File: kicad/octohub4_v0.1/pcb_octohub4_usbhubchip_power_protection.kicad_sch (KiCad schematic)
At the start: 16 parts, among them J201 Screw_Terminal_01x02, J203 Barrel_Jack_Switch, U201 TPS259474LRPWR

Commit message: Add run_kicad_purge 2
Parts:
- added JP201, JP202: SolderJumper_2_Bridged, Jumper:SolderJumper-2_P1.3mm_Bridged_RoundedPad1.0x1.5mm, symbol Jumper:SolderJumper_2_Bridged
- added JP205: SolderJumper_2_Open, Jumper:SolderJumper-2_P1.3mm_Open_RoundedPad1.0x1.5mm, symbol Jumper:SolderJumper_2_Open
- added TH1301, TH1302: JLCPCB Tooling Hole, 00_project_library:JLCPCB_ToolingHole, symbol 00_project_library:JLCPCB_ToolingHole
- BP201, BP202: footprint SolderWirePad_1x01_SMD_2x4mm -> Connector_Wire:SolderWirePad_1x01_SMD_2x4mm
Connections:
- net +5VIN: now also JP201.1 (A), JP202.1 (A), JP205.2 (B); no longer H201.1, H202.1
- net +5VOUT renamed +5VPROTECTED
- net +5VPROTECTED: now also JP205.1 (A)
- new net: H202.1, JP202.2 (B)
- new net: H201.1, JP201.2 (B)
- no-connect marks 0 -> 2
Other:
- moved on the sheet: H1301, H1302, H201, H202

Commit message: Add run_kicad_purge 3
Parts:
- added D207: green, LED_SMD:LED_0805_2012Metric, symbol 00_project_library:LED GREEN
- added R202: 4K7, Resistor_SMD:R_0805_2012Metric, symbol Device:R
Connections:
- net +5VIN: now also J201.2 (Pin_2); no longer J201.1 (Pin_1)
- net +5VPROTECTED: now also R202.2
- net GND: now also J201.1 (Pin_1), D207.1 (K); no longer J201.2 (Pin_2)
- new net: D207.2 (A), R202.1
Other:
- note added: "5VPROTECTED LED"
- moved on the sheet: J201

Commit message: Add run_kicad_purge 4
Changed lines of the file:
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@@
-	(wire
-		(pts
-			(xy 80.01 97.79) (xy 80.01 102.87)
-		)
-		(stroke
-			(width 0)
-			(type default)
-		)
-	)
 	(wire
 		(pts

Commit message: Add run_kicad_purge 5
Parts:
- J201: now left out of the parts list
- R201: value 137 -> 120
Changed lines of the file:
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@@
 		)
 	)
-	(text_box "R201: Current limit ~4.47A (612 / 137 Ohm)\nC203: Allows transient surges (up to 2x limit) for ~6ms.\nC202: Output voltage ramp time to 5V/500ms"
+	(text_box "R201: Current limit ~5.1A (612 / 120 Ohm)\nC203: Allows transient surges (up to 2x limit) for ~6ms.\nC202: Output voltage ramp time to 5V/500ms"
 		(exclude_from_sim no)
 		(at 92.71 128.27 0)
@@
 			)
 		)
-		(property "Value" "137"
+		(property "Value" "120"
 			(at 158.6484 111.76 90)
 			(effects
@@
 		(unit 1)
 		(exclude_from_sim no)
-		(in_bom yes)
-		(on_board yes)
-		(dnp no)
+		(in_bom no)
+		(on_board yes)
+		(dnp no)

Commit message: Add run_kicad_purge 6
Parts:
- J203: now left out of the parts list
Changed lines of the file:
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@@
 		(unit 1)
 		(exclude_from_sim no)
-		(in_bom yes)
+		(in_bom no)
 		(on_board yes)
 		(dnp no)

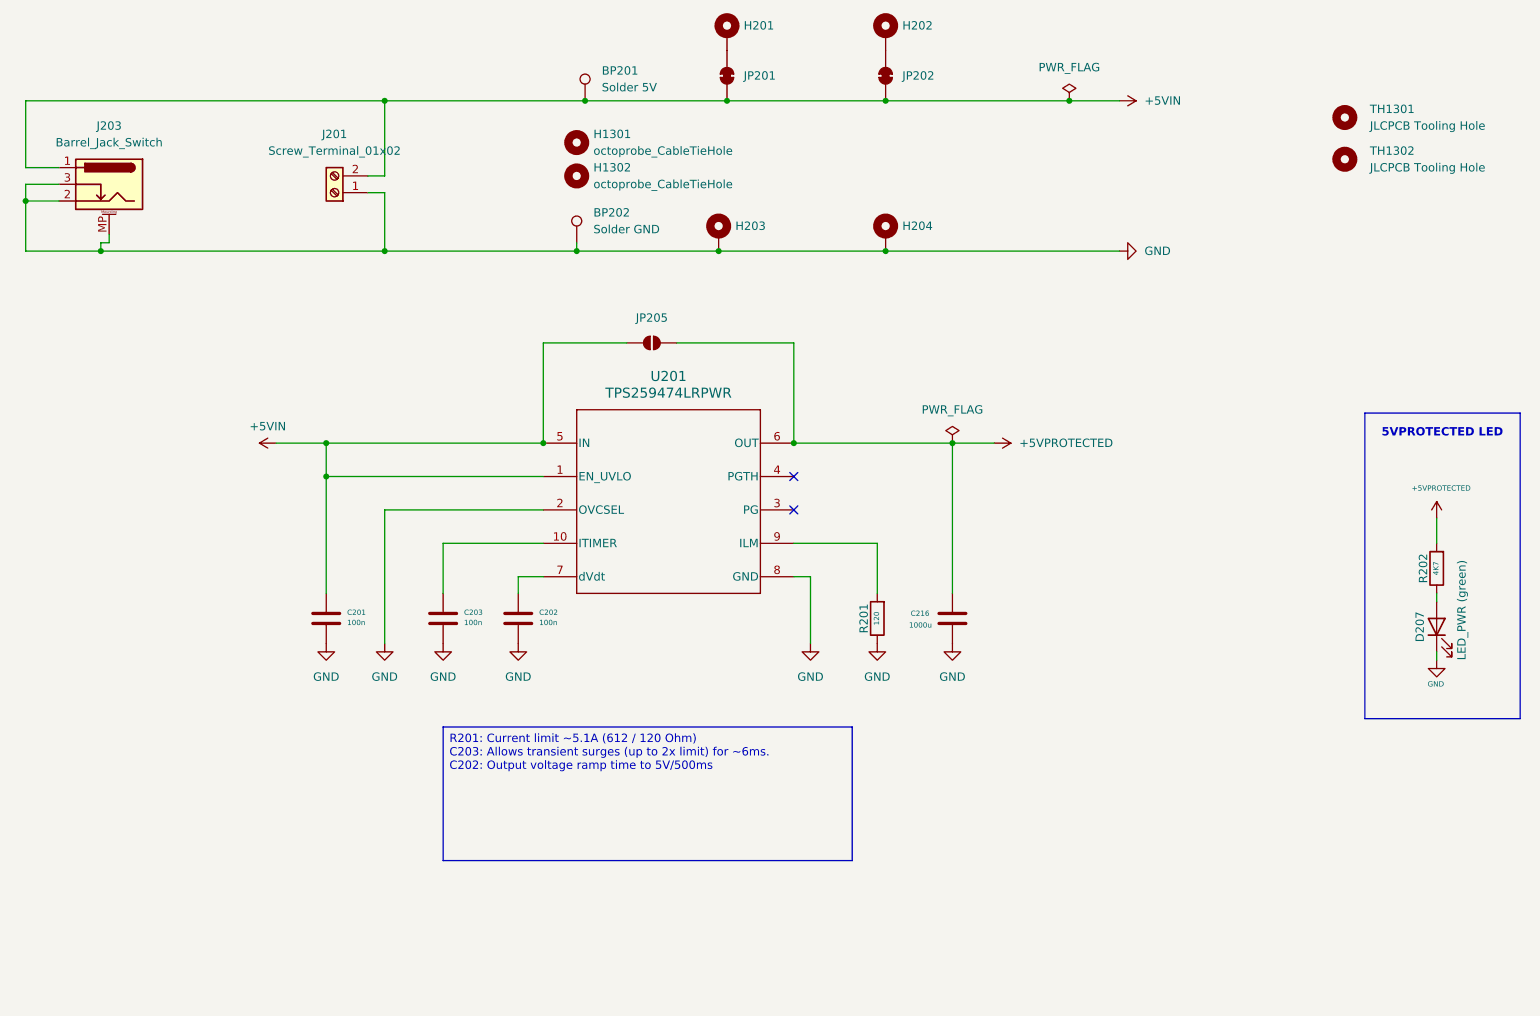
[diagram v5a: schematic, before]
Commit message: Add run_kicad_purge 9
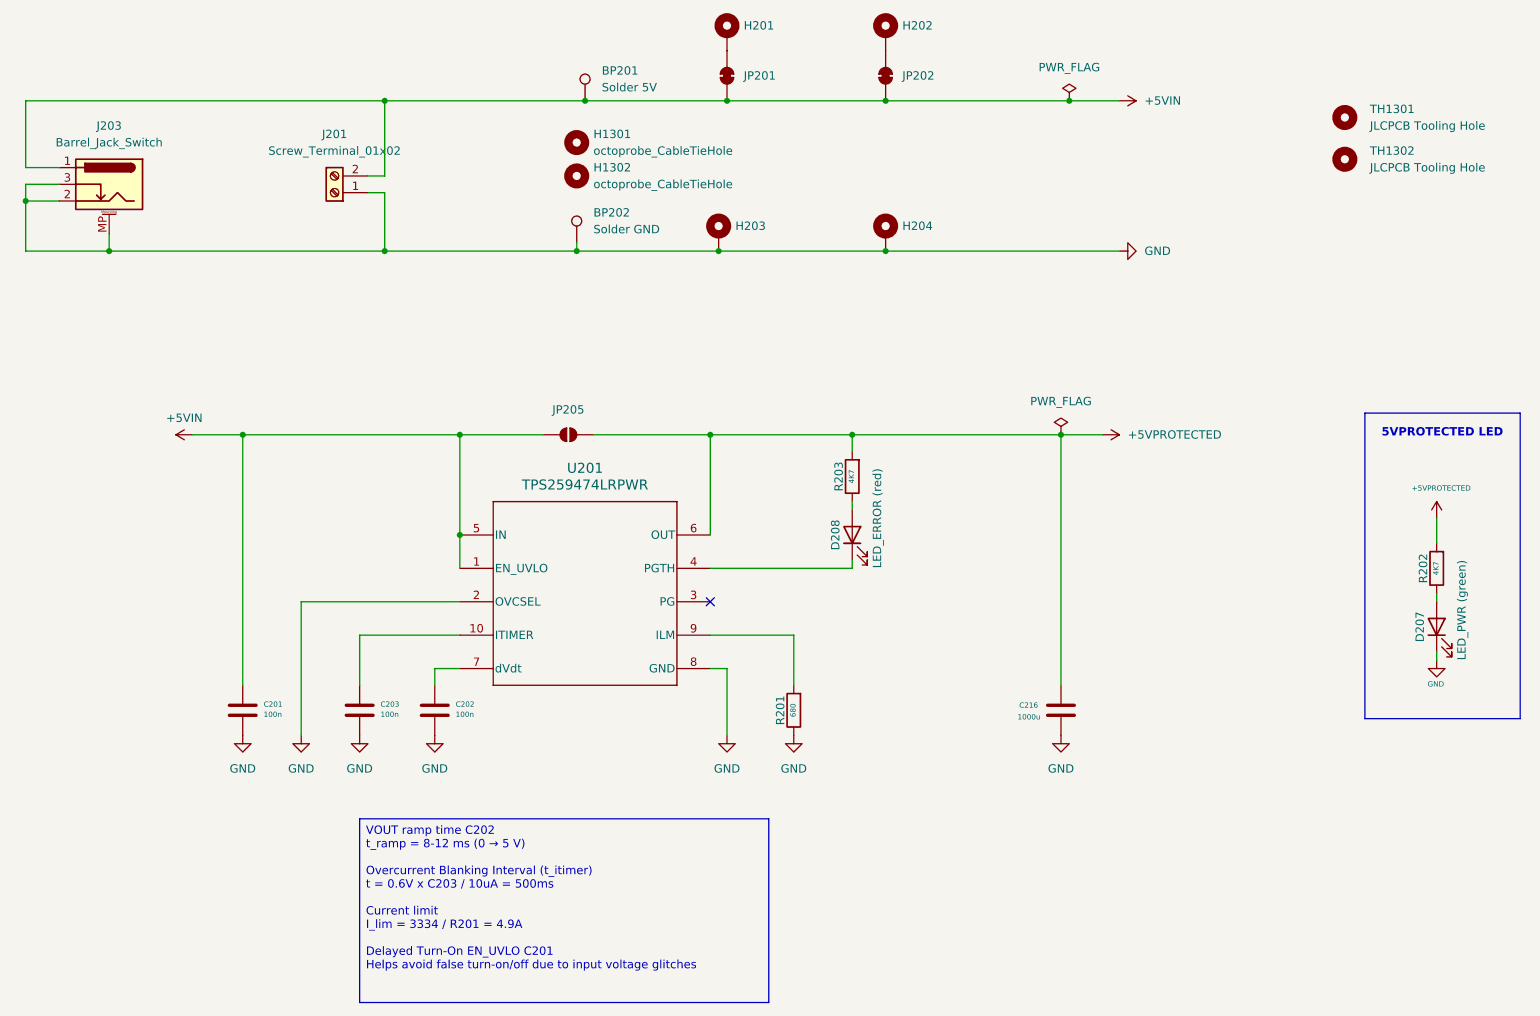
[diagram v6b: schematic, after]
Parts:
- added D208: green, LED_SMD:LED_0805_2012Metric, symbol 00_project_library:LED RED
- added R203: 4K7, Resistor_SMD:R_0805_2012Metric, symbol Device:R
- R201: value 120 -> 680
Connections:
- net +5VPROTECTED: now also R203.2
- net at U201.4 (PGTH): now also D208.1 (K)
- new net: D208.2 (A), R203.1
- no-connect marks 2 -> 1
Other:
- moved on the sheet: C201, C202, C203, C216, JP205, R201, U201
